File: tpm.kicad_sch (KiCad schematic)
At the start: 0 parts

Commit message: [#99732] Implement TPM schematic
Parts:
- added C801: C_100n_0402, antmicro-footprints:C_0402_1005Metric, symbol antmicroCapacitors0402:C_100n_0402
- added J801: PinHeader_2x7_P2mm_MTMM-107-05-L-D-195-014, antmicro-footprints:PinHeader_2x7_P2mm_Drill0.9mm_MTMM, symbol antmicroGenericPinHeaders:PinHeader_2x7_P2mm_MTMM-107-05-L-D-195-014
- added R801, R802, R803: R_0R_0402, antmicro-footprints:R_0402_1005Metric, symbol antmicroResistors0402:R_0R_0402
- added U801: TS3A27518E_QFN, antmicro-footprints:QFN-24-1EP_4x4mm_P0.5mm_EP2.6x2.6mm, symbol antmicroInterfaceAnalogSwitchesMultiplexersDemultiplexers:TS3A27518E_QFN
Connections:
- new net: R801.2, U801.11 (IN2), U801.21 (IN1)
- new net: J801.3, R802.1, R803.1
- new net +1V8: C801.2, J801.1, R803.2, U801.5 (VCC)
- new net DC-SCM-SPI.DI: U801.23 (NC1)
- new net DC-SCM-SPI.DO: U801.22 (NC2)
- new net DC-SCM-SPI.SCK: U801.20 (NC3)
- new net DC-SCM-SPI.~{CS0}: U801.18 (NC4)
- new net GND: C801.1, J801.8, U801.17 (~{EN}), U801.2 (GND), U801.25 (EP)
- new net OSM_SPI.DI: U801.8 (NO1)
- new net OSM_SPI.DO: U801.10 (NO2)
- new net OSM_SPI.SCK: U801.12 (NO3)
- new net OSM_SPI.~{CS0}: U801.14 (NO4)
- new net TPM_MUX_SEL: R801.1
- new net TPM_SPI.DI: J801.11, U801.1 (COM1)
- new net TPM_SPI.DO: J801.12, U801.3 (COM2)
- new net TPM_SPI.SCK: J801.10, U801.4 (COM3)
- new net TPM_SPI.~{CS0}: J801.4, U801.6 (COM4)
- new net ~{PIRQ}: J801.2
- new net ~{RST}: R802.2
- no-connect marks 0 -> 12

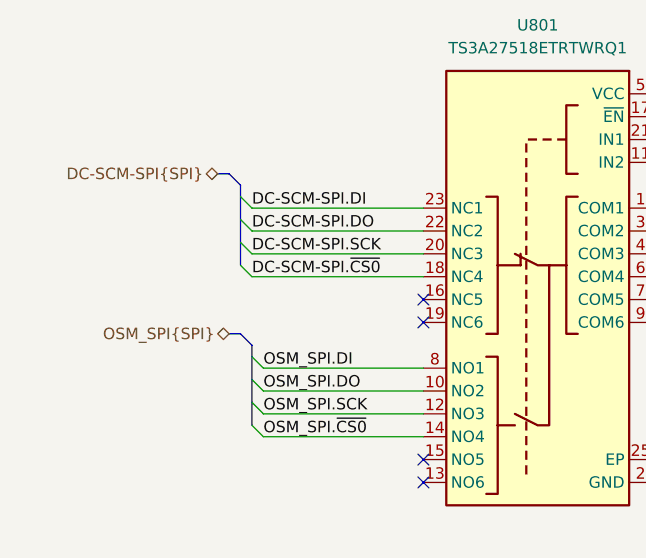
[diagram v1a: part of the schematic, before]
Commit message: [#99732] Rename TPM SPI buses, import them on root schematic
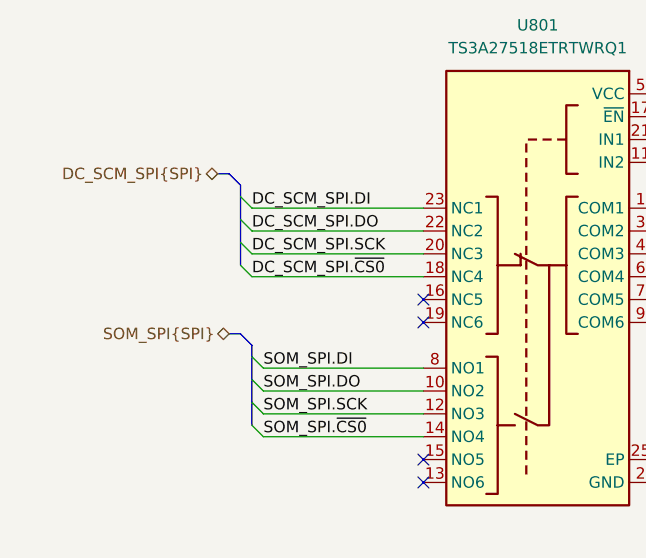
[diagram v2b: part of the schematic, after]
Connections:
- net DC-SCM-SPI.DI renamed DC_SCM_SPI.DI
- net DC-SCM-SPI.DO renamed DC_SCM_SPI.DO
- net DC-SCM-SPI.SCK renamed DC_SCM_SPI.SCK
- net DC-SCM-SPI.~{CS0} renamed DC_SCM_SPI.~{CS0}
- net OSM_SPI.DI renamed SOM_SPI.DI
- net OSM_SPI.DO renamed SOM_SPI.DO
- net OSM_SPI.SCK renamed SOM_SPI.SCK
- net OSM_SPI.~{CS0} renamed SOM_SPI.~{CS0}
